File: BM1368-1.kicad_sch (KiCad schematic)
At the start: 39 parts, among them U10 BM1368_mode1, U11 BM1368_mode1

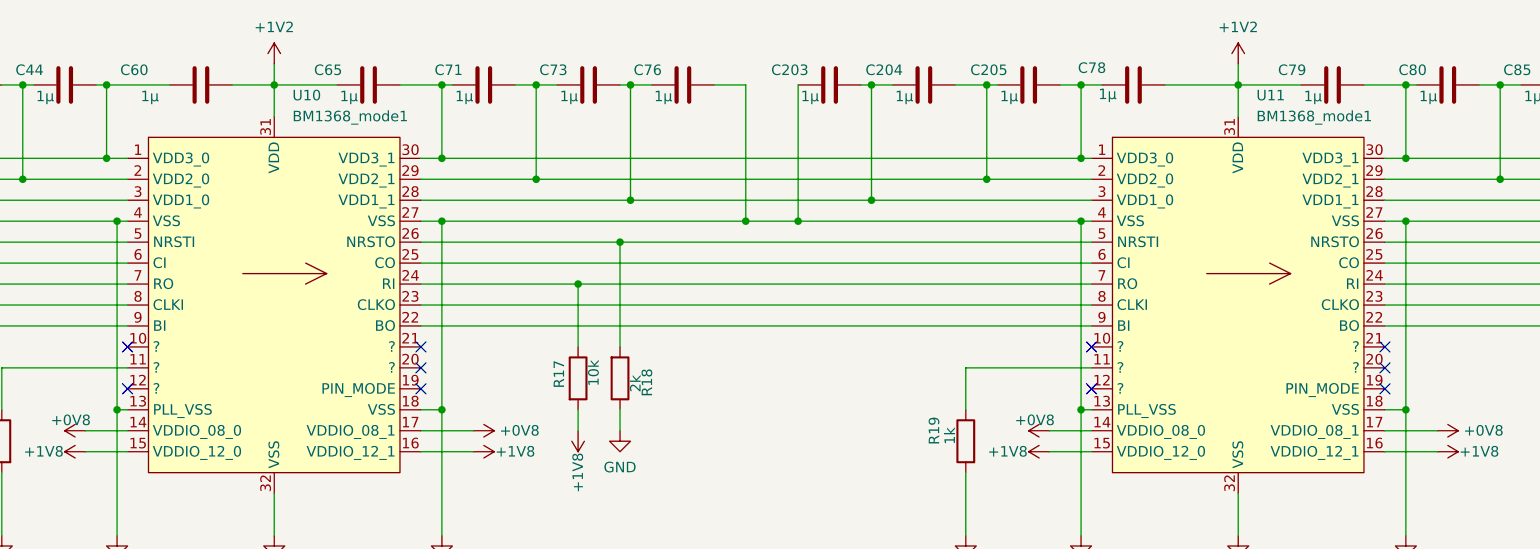
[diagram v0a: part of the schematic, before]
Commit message: Added 4th Phase Buck
Started to add 4th Phase for the Buck, implementing BM1370 footprint etc
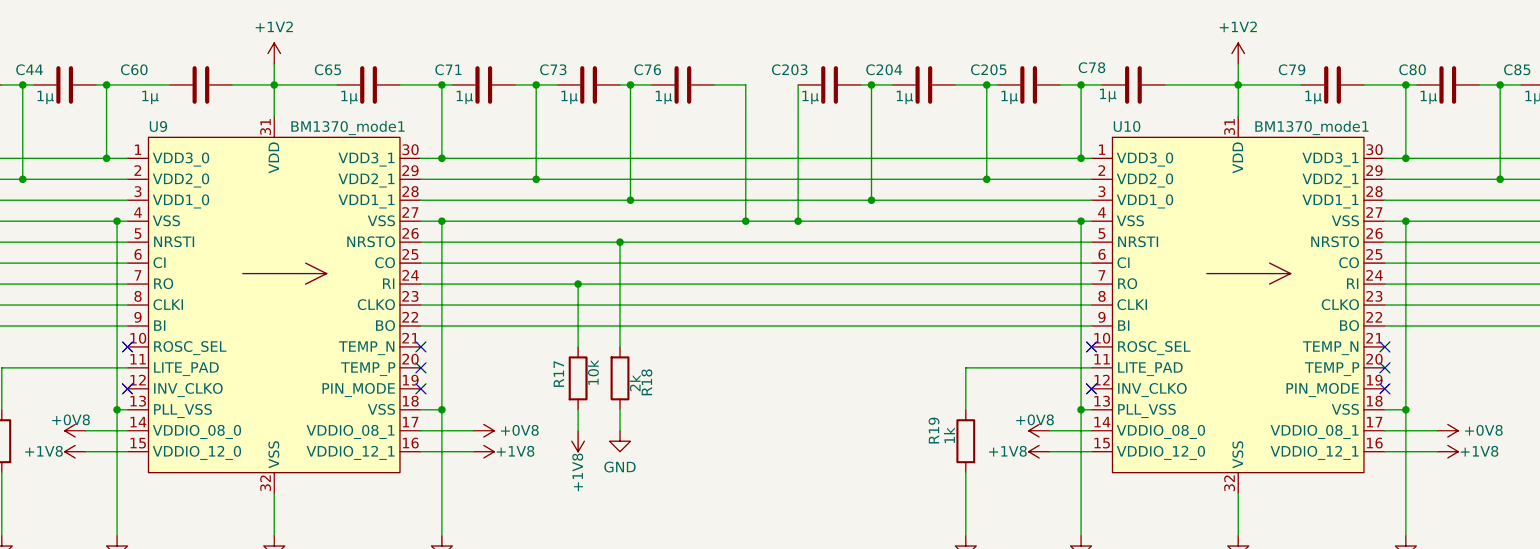
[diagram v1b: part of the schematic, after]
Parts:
- removed U10, U11: BM1368_mode1, myfootprints:bm1368-package-modified, symbol mylib7:BM1368_mode1
- added U10, U9: BM1370_mode1, Nerd8:BM1370, symbol bitaxe:BM1370_mode1
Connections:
- net +0V8: now also U10.14 (VDDIO_08_0), U10.17 (VDDIO_08_1), U9.14 (VDDIO_08_0), U9.17 (VDDIO_08_1)
- net +1V2: now also U10.31 (VDD), U9.31 (VDD)
- net +1V8: now also U10.15 (VDDIO_12_0), U10.16 (VDDIO_12_1), U9.15 (VDDIO_12_0), U9.16 (VDDIO_12_1)
- net BI: now also U9.9 (BI)
- net BO: now also U10.22 (BO)
- net CI: now also U9.6 (CI)
- net CLKI: now also U9.8 (CLKI)
- net CLKO: now also U10.23 (CLKO)
- net CO: now also U10.25 (CO)
- net GND: now also U10.13 (PLL_VSS), U10.18 (VSS), U10.27 (VSS), U10.32 (VSS), U10.4 (VSS), U9.13 (PLL_VSS), U9.18 (VSS), U9.27 (VSS), U9.32 (VSS), U9.4 (VSS)
- net NRSTI: now also U9.5 (NRSTI)
- net NRSTO: now also U10.26 (NRSTO)
- net RI: now also U10.24 (RI)
- net RO: now also U9.7 (RO)
- net U11-VDD1_1: now also U10.28 (VDD1_1)
- net U11-VDD2_1: now also U10.29 (VDD2_1)
- net U11-VDD3_1: now also U10.30 (VDD3_1)
- net U9-VDD1_1: now also U9.3 (VDD1_0)
- net U9-VDD2_1: now also U9.2 (VDD2_0)
- net U9-VDD3_1: now also U9.1 (VDD3_0)
- net at C205.2, C65.2, C71.1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: now also U10.1 (VDD3_0), U9.30 (VDD3_1)
- net at C204.2, C205.1, C71.2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: now also U10.2 (VDD2_0), U9.29 (VDD2_1)
- net at C203.2, C204.1, C73.2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: now also U10.3 (VDD1_0), U9.28 (VDD1_1)
- net at R19.1: now also U10.11 (LITE_PAD)
- net at R18.2: now also U10.5 (NRSTI), U9.26 (NRSTO)
- net at R17.1: now also U10.7 (RO), U9.24 (RI)
- net at R16.1: now also U9.11 (LITE_PAD)
- new net: U10.9 (BI), U9.22 (BO)
- new net: U10.8 (CLKI), U9.23 (CLKO)
- new net: U10.6 (CI), U9.25 (CO)

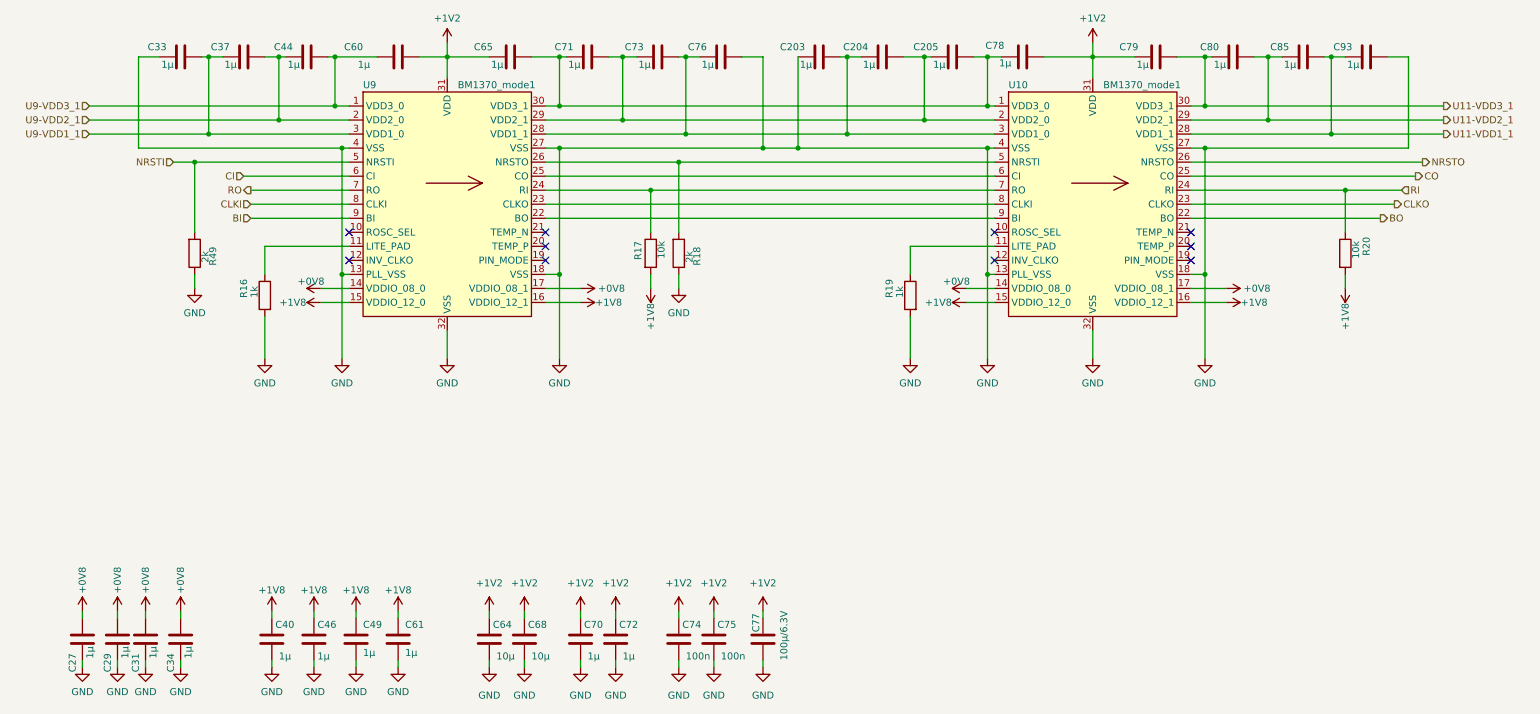
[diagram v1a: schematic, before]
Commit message: Changed LDO to 1V2 and original 1V2 to VDD
1V8 LDO replaced with 1V2 LDO
Crystal replaced
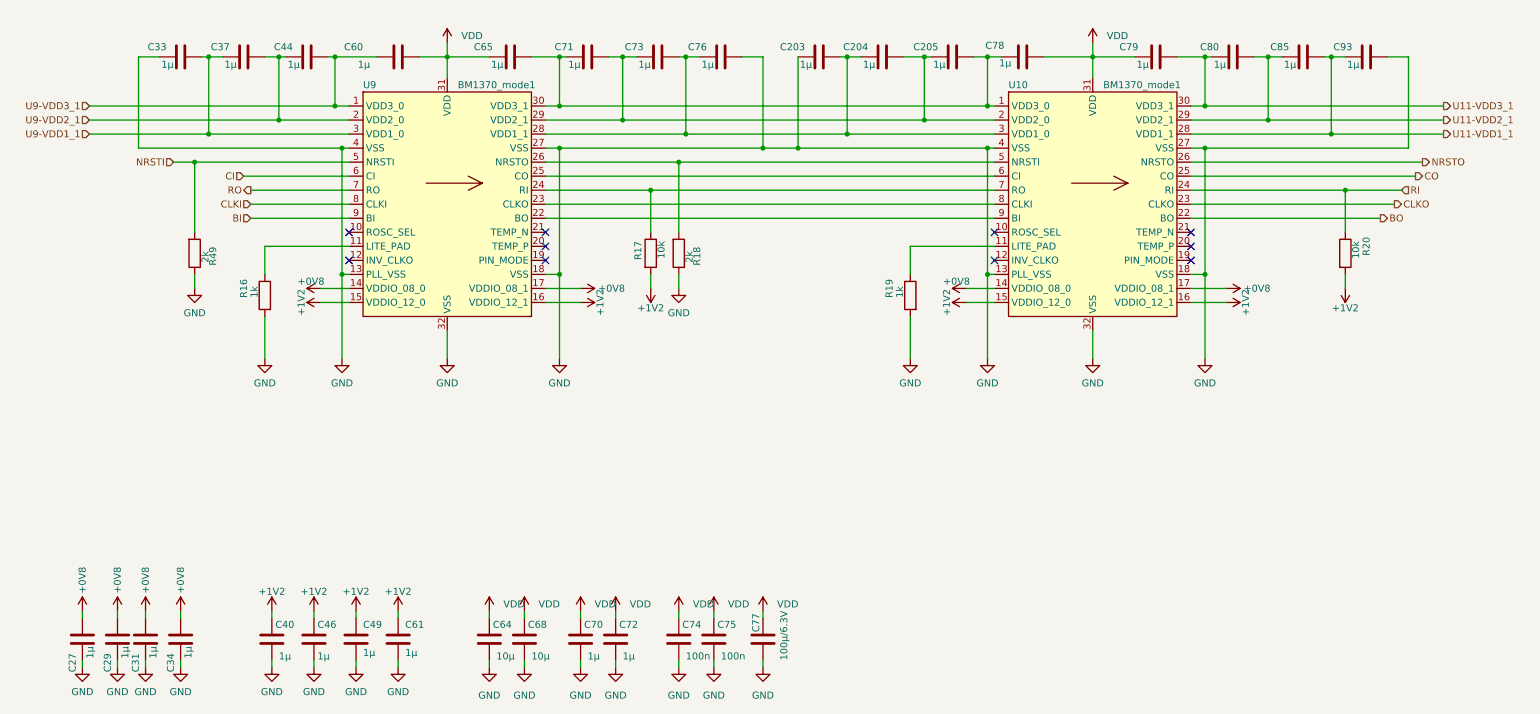
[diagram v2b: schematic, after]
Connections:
- net +1V8 is gone; now on net +1V2: C40.1, C46.1, C49.1, C61.1, R17.2, R20.2, U10.15 (VDDIO_12_0), U10.16 (VDDIO_12_1), U9.15 (VDDIO_12_0), U9.16 (VDDIO_12_1)
- net +1V2: no longer C60.2, C64.1, C65.1, C68.1, C70.1, C72.1, C74.1, C75.1, C77.1, C78.2, C79.1, U10.31 (VDD), U9.31 (VDD)
- new net VDD: C60.2, C64.1, C65.1, C68.1, C70.1, C72.1, C74.1, C75.1, C77.1, C78.2, C79.1, U10.31 (VDD), U9.31 (VDD)

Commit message: BOM changes
1nF  to 1nF 0.7mm etc
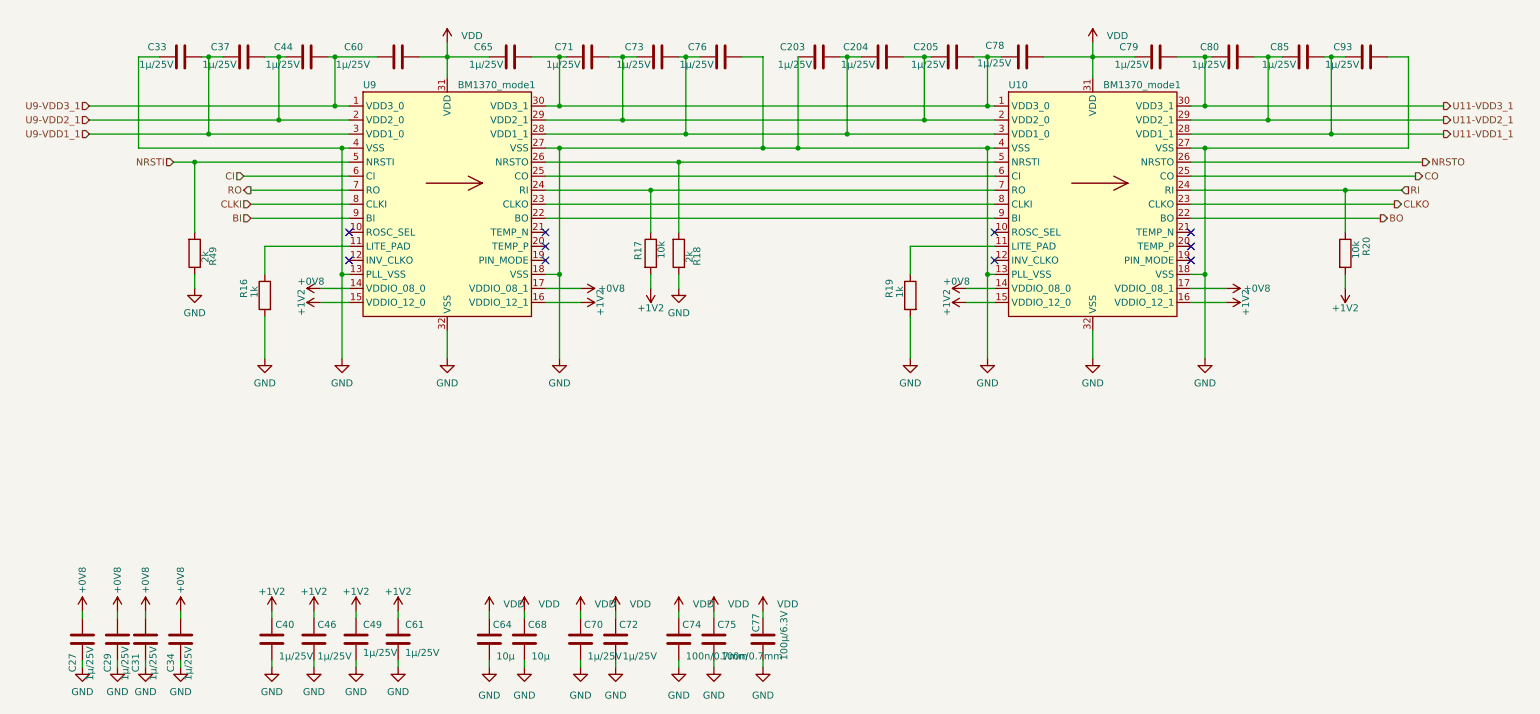
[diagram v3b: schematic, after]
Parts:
- C203, C204, C205, C27, C29, C31, C33, C34, C37, C40, C44, C46, C49, C60, C61, C65, C70, C71, C72, C73, C76, C78, C79, C80, C85, C93: value 1µ -> 1µ/25V; Distributor (none) -> D; Manufacturer (none) -> CL21B105KAFNNNE; OrderNr (none) -> 1276-1066-1-ND
- C74, C75: value 100n -> 100n/0.7mm; Distributor (none) -> D; Manufacturer (none) -> AC0805KRX7R9BB104; OrderNr (none) -> 311-3037-1-ND
- R16, R19: Distributor (none) -> D; Manufacturer (none) -> RNCP0805FTD1K00; OrderNr (none) -> RNCP0805FTD1K00CT-ND
- R17, R20: Distributor (none) -> D; Manufacturer (none) -> RMCF0805FT10K0; OrderNr (none) -> RMCF0805FT10K0CT-ND
- R18, R49: Distributor (none) -> D; Manufacturer (none) -> CRG0805F2K0; OrderNr (none) -> A126358CT-ND
- U10, U9: Manufacturer (none) -> BM1370 BITMAIN; OrderNr (none) -> -
